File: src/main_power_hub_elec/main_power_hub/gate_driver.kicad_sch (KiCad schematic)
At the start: 3 parts, among them Q2 NPN, Q3 NMOS

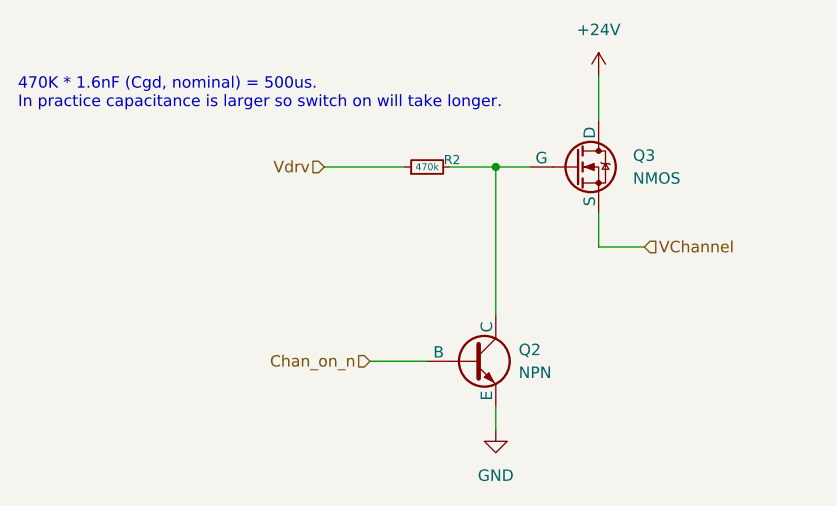
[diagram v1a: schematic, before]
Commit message: Wire channels on schematic
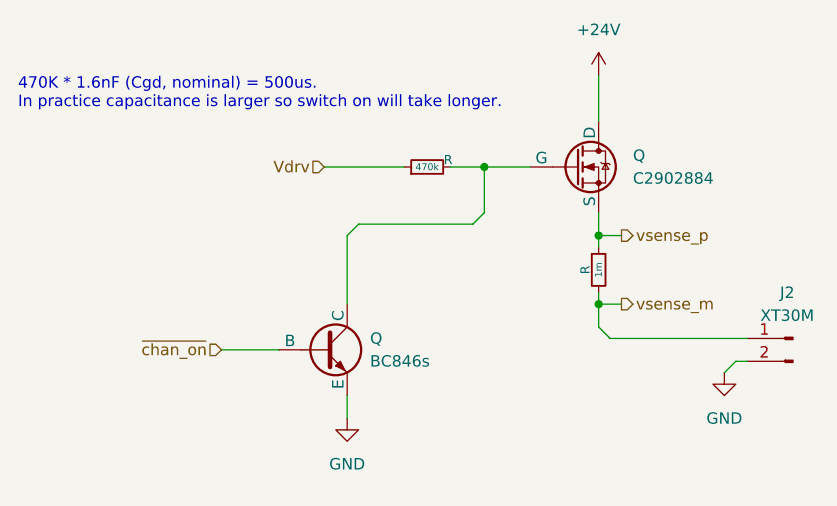
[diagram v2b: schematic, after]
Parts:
- added J2: XT30M, symbol Connector:Conn_01x02_Pin
- added R: 1m, symbol Bluesat:R_CompactV
- Q: renamed from Q2; value NPN -> BC846s
- Q: renamed from Q3; value NMOS -> C2902884
- renumbered R2 to R
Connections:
- net GND: now also J2.2 (Pin_2)
- net Chan_on_n renamed ~{chan_on}
- net VChannel renamed vsense_p
- net vsense_p: now also R.1
- new net vsense_m: J2.1 (Pin_1), R.2
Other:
- moved on the sheet: Q

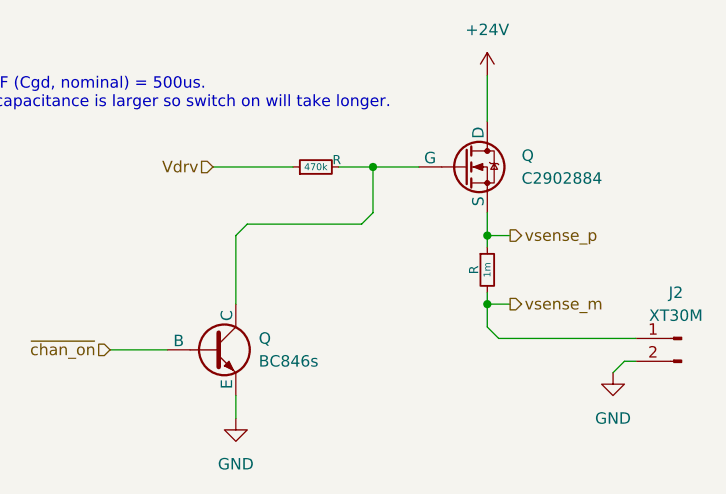
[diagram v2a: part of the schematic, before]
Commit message: Add crystal, swdio header, other misc board stuff to MPM
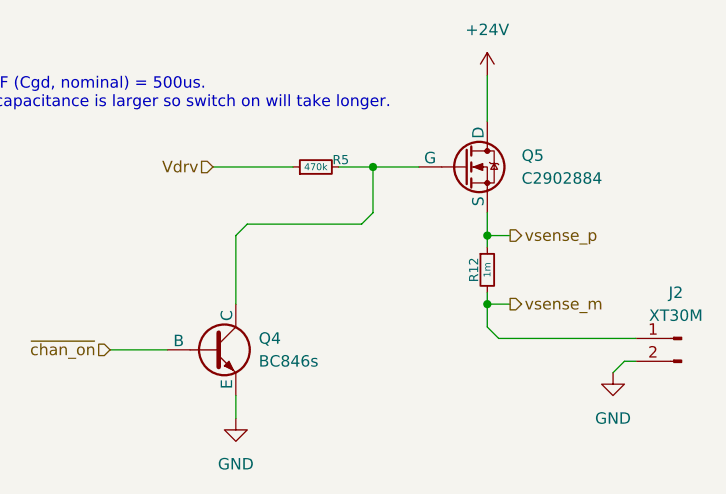
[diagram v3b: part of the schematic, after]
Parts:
- renumbered Q to Q4, Q to Q5, R to R12, R to R5
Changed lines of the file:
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@@
 		(dnp no)
 		(fields_autoplaced yes)
-		(property "Reference" "Q"
+		(property "Reference" "Q4"
 			(at 100.33 87.6299 0)
 			(effects
@@
 				(path "/535f321e-8428-4dab-8e55-8d6d7e9876bc/c36d76ea-44e9-4d64-b46e-ad2297433d21"
 					(reference "Q2")
+					(unit 1)
+				)
+				(path "/535f321e-8428-4dab-8e55-8d6d7e9876bc/d7476164-5218-41ec-b025-95e58a333636"
+					(reference "Q4")
 					(unit 1)
 				)
@@
 		(dnp no)
 		(fields_autoplaced yes)
-		(property "Reference" "#PWR"
+		(property "Reference" "#PWR035"
 			(at 125.73 62.23 0)
 			(effects
@@
 				(path "/535f321e-8428-4dab-8e55-8d6d7e9876bc/c36d76ea-44e9-4d64-b46e-ad2297433d21"
 					(reference "#PWR018")
+					(unit 1)
+				)
+				(path "/535f321e-8428-4dab-8e55-8d6d7e9876bc/d7476164-5218-41ec-b025-95e58a333636"
+					(reference "#PWR035")
 					(unit 1)
 				)
@@
 		(dnp no)
 		(fields_autoplaced yes)
-		(property "Reference" "Q"
+		(property "Reference" "Q5"
 			(at 129.54 67.3099 0)
 			(effects
@@
 				(path "/535f321e-8428-4dab-8e55-8d6d7e9876bc/c36d76ea-44e9-4d64-b46e-ad2297433d21"
 					(reference "Q3")
+					(unit 1)
+				)
+				(path "/535f321e-8428-4dab-8e55-8d6d7e9876bc/d7476164-5218-41ec-b025-95e58a333636"
+					(reference "Q5")
 					(unit 1)
 				)
@@
 		(dnp no)
 		(fields_autoplaced yes)
-		(property "Reference" "#PWR"
+		(property "Reference" "#PWR034"
 			(at 97.79 102.87 0)
 			(effects
@@
 				(path "/535f321e-8428-4dab-8e55-8d6d7e9876bc/c36d76ea-44e9-4d64-b46e-ad2297433d21"
 					(reference "#PWR06")
+					(unit 1)
+				)
+				(path "/535f321e-8428-4dab-8e55-8d6d7e9876bc/d7476164-5218-41ec-b025-95e58a333636"
+					(reference "#PWR034")
 					(unit 1)
 				)
@@
 		(dnp no)
 		(fields_autoplaced yes)
-		(property "Reference" "R"
+		(property "Reference" "R5"
 			(at 108.5215 68.3895 0)
 			(do_not_autoplace yes)
@@
 				(path "/535f321e-8428-4dab-8e55-8d6d7e9876bc/c36d76ea-44e9-4d64-b46e-ad2297433d21"
 					(reference "R6")
+					(unit 1)
+				)
+				(path "/535f321e-8428-4dab-8e55-8d6d7e9876bc/d7476164-5218-41ec-b025-95e58a333636"
+					(reference "R5")
 					(unit 1)
 				)
@@
 		(dnp no)
 		(fields_autoplaced yes)
-		(property "Reference" "R"
+		(property "Reference" "R12"
 			(at 124.841 80.01 90)
 			(do_not_autoplace yes)
@@
 					(unit 1)
 				)
+				(path "/535f321e-8428-4dab-8e55-8d6d7e9876bc/d7476164-5218-41ec-b025-95e58a333636"
+					(reference "R12")
+					(unit 1)
+				)

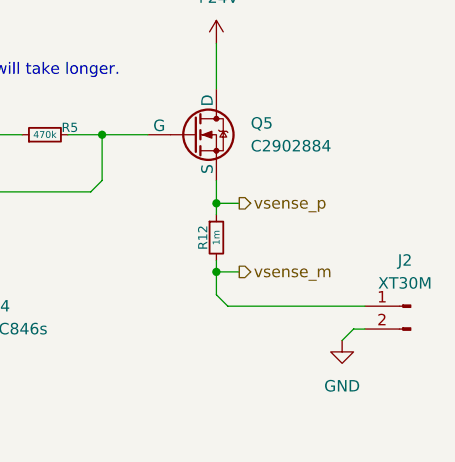
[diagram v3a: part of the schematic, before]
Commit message: Fix bypass cap grounding, add estop on charge pump, fix pin naming on MCU.
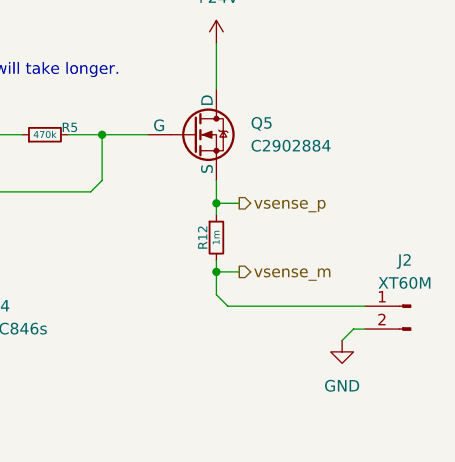
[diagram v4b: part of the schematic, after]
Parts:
- J2: value XT30M -> XT60M
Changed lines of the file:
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@@
 			)
 		)
-		(property "Value" "XT30M"
+		(property "Value" "XT60M"
 			(at 146.685 85.09 0)
 			(effects

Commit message: Make the bus real
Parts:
- added C19: 100n, symbol Bluesat:C_CompactH
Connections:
- net GND: now also C19.1
- net at Q4.1 (C), Q5.2 (G), R5.2: now also C19.2
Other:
- note added: "470K * 100nF = 50ms."
- note removed: "470K * 1.6nF (Cgd, nominal) = 500us. In practice capacitance is larger so switch on will take longer."
- moved on the sheet: Q4, R5

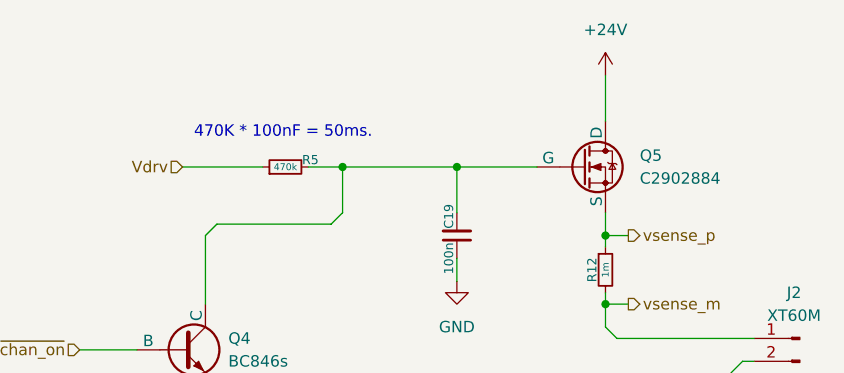
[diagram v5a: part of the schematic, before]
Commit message: Do switch on time calculation
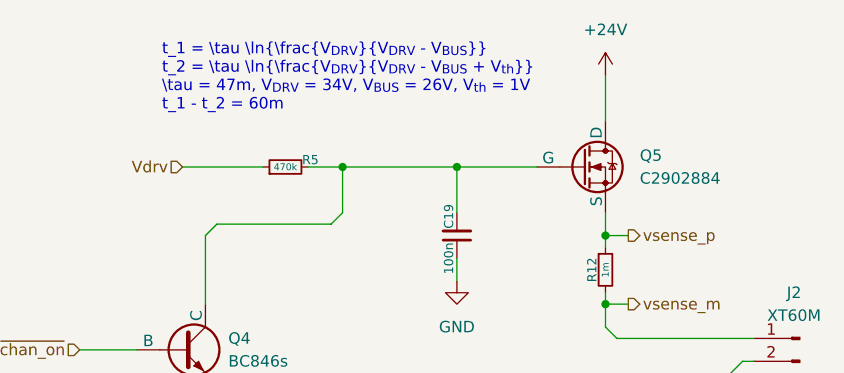
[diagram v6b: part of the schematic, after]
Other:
- note added: "t_1 = \tau \ln{\frac{V_{DRV}}{V_{DRV} - V_{BUS}}} t_2 = \tau \ln{\frac{V_{DRV}}{V_{DRV} - V_{BUS} + V_{th}}} \tau = 47m, V_{DRV} = 34V, V_{BUS} = 26V, V_{th} = 1V t_1 - t_2 = 60m"
- note removed: "470K * 100nF = 50ms."
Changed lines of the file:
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@@
 	(generator_version "9.0")
 	(paper "A4")
-	(text "470K * 100nF = 50ms."
+	(text "t_1 = \\tau \\ln{\\frac{V_{DRV}}{V_{DRV} - V_{BUS}}}\nt_2 = \\tau \\ln{\\frac{V_{DRV}}{V_{DRV} - V_{BUS} + V_{th}}}\n\\tau = 47m, V_{DRV} = 34V, V_{BUS} = 26V, V_{th} = 1V\nt_1 - t_2 = 60m\n"
 		(exclude_from_sim no)
-		(at 80.01 64.77 0)
+		(at 76.454 58.674 0)
 		(effects
 			(font

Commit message: Schematic done (?)
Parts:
- removed Q4: BC846s, symbol Simulation_SPICE:NPN
- removed Q5: C2902884, symbol Simulation_SPICE:NMOS
- removed R12: 1m, symbol Bluesat:R_CompactV
- added C10, C11, C38, C39, C40, C41, C8, C9: 1n, symbol Bluesat:C_CompactV
- added C21, C31, C34, C35: 1n, symbol Bluesat:C_CompactH
- added C22, C32, C33: 100n, symbol Bluesat:C_CompactH
- added C36: 100n, symbol Bluesat:C_CompactV
- added C37: 1u, symbol Bluesat:C_CompactV
- added D11, D12: SBR0560S1-7, symbol Device:D_Schottky
- added J3: JST_PA-2-P, symbol Connector:Conn_01x02_Pin
- added J4, J5, J7: XT60M, symbol Connector:Conn_01x02_Pin
- added Q1: SSM3K333R, symbol Transistor_FET:Q_NMOS_DGS
- added Q2, Q3, Q5, Q7: IRFH7440TRPBF, Bluesat:PQFN_5x6mm_E_SGD, symbol Transistor_FET:Q_NMOS_SGD
- added Q4, Q6: Q_Dual_NPN_NPN_E1B1C2E2B2C1, Package_TO_SOT_SMD:SOT-363_SC-70-6, symbol Transistor_BJT:Q_Dual_NPN_NPN_E1B1C2E2B2C1
- added R10, R20, R24, R25: 1m, symbol Bluesat:R_CompactV
- added R11, R6, R7: 10k, symbol Bluesat:R_CompactH
- added R12, R17, R18, R9: 470k, symbol Bluesat:R_CompactH
- added R19: 470k, symbol Bluesat:R_CompactV
- added R8: 100R, symbol Bluesat:R_CompactH
- R5: value 470k -> 10k
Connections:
- net GND: now also C11.1, C21.2, C22.1, C31.2, C32.1, C33.1, C34.2, C35.2, C37.1, C39.1, C41.1, C9.1, Q1.3 (S), Q4.1 (E1), Q4.4 (E2), Q6.1 (E1), Q6.4 (E2), R10.2, R19.2, R20.2, R24.2, R25.2; no longer J2.2 (Pin_2)
- net at R5.2: now also Q4.2 (B1); no longer C19.2
- net Vdrv renamed ~{chan2}
- net vsense_m renamed vsense_p2
- net vsense_p2: now also C10.1, C11.2, R24.1
- new net: C33.2, Q4.3 (C2), Q5.2 (G), R18.2
- new net: C36.1, Q1.1 (D), R8.2
- new net: C38.2, J5.2 (Pin_2), Q5.1 (S)
- new net: C8.2, J4.2 (Pin_2), Q3.1 (S)
- new net: C22.2, Q3.2 (G), Q6.6 (C1), R9.2
- new net: C32.2, Q2.2 (G), Q4.6 (C1), R17.2
- new net: C40.2, J7.2 (Pin_2), Q7.1 (S)
- new net: Q6.2 (B1), R6.2
- new net: C10.2, J2.2 (Pin_2), Q2.1 (S)
- new net: C19.2, Q6.3 (C2), Q7.2 (G), R12.2
- new net: Q6.5 (B2), R11.2
- new net: Q4.5 (B2), R7.2
- new net: C36.2, D11.1 (K), D12.2 (A)
- new net: D12.1 (K), J3.2 (Pin_2)
- new net +12V: R8.1
- new net VBUS: C21.1, C31.1, C34.1, C35.1, D11.2 (A), Q2.3 (D), Q3.3 (D), Q5.3 (D), Q7.3 (D)
- new net Vdrive: C37.2, J3.1 (Pin_1), R12.1, R17.1, R18.1, R19.1, R9.1
- new net clk_in: Q1.2 (G)
- new net vsense_p0: C8.1, C9.2, J4.1 (Pin_1), R10.1
- new net vsense_p1: C40.1, C41.2, J7.1 (Pin_1), R20.1
- new net vsense_p3: C38.1, C39.2, J5.1 (Pin_1), R25.1
- new net ~{chan0}: R6.1
- new net ~{chan1}: R11.1
- new net ~{chan3}: R7.1
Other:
- note added: "30V"
- note added: "50V"
- note added: "Assume diode behaviour, i.e. exponential. From the data sheet, resistance is proportional to e^20t. Take 1V range as being "linear region." Solving with RC we get 30ms."
- note added: "Charge Pump"
- note added: "Switching"
- note added: "Works in sim source: trust me bro"
- note removed: "t_1 = \tau \ln{\frac{V_{DRV}}{V_{DRV} - V_{BUS}}} t_2 = \tau \ln{\frac{V_{DRV}}{V_{DRV} - V_{BUS} + V_{th}}} \tau = 47m, V_{DRV} = 34V, V_{BUS} = 26V, V_{th} = 1V t_1 - t_2 = 60m"

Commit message: Fixed jethro stuff NEED FOOTPRINTS
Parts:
- removed C10, C11, C38, C39, C40, C41, C8, C9: 1n, symbol Bluesat:C_CompactV
- removed C19, C22, C32, C33: 100n, symbol Bluesat:C_CompactH
- removed C21, C31, C34, C35: 1n, symbol Bluesat:C_CompactH
- removed J2, J4, J5, J7: XT60M, symbol Connector:Conn_01x02_Pin
- removed Q2, Q3, Q5, Q7: IRFH7440TRPBF, Bluesat:PQFN_5x6mm_E_SGD, symbol Transistor_FET:Q_NMOS_SGD
- removed Q4, Q6: Q_Dual_NPN_NPN_E1B1C2E2B2C1, Package_TO_SOT_SMD:SOT-363_SC-70-6, symbol Transistor_BJT:Q_Dual_NPN_NPN_E1B1C2E2B2C1
- removed R10, R20, R24, R25: 1m, symbol Bluesat:R_CompactV
- removed R11, R5, R6, R7: 10k, symbol Bluesat:R_CompactH
- removed R12, R17, R18, R9: 470k, symbol Bluesat:R_CompactH
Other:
- added sheet Mosfets 1 (mosfets.kicad_sch)
- added sheet Mosfets 2 (mosfets.kicad_sch)
